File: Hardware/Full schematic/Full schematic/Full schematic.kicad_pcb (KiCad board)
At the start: 2 copper layers, 128 x 62.4 mm, 163 parts, among them J1 Conn_01x04_Male, J2 Conn_01x03_Male, J3 Conn_01x02_Male, J4 Conn_01x04_Male, J5 Conn_01x03_Male, J6 Conn_01x02_Male, J7 Conn_01x02_Male, J8 Conn_01x02_Male, J9 Conn_01x07_Male, K1 EDR101A0500, K2 EDR101A0500, K3 EDR101A0500, K4 EDR101A0500, K5 EDR101A0500, K6 EDR101A0500, Q1 BC847, Q10 IRLML2502, Q11 IRLML2502, Q12 IRLML2502, Q13 IRLML2502, Q2 BSS138, Q3 BC847, Q4 IRF610, Q5 BSS138, Q6 BFS17, Q7 AFT05MS003N, Q8 IRLML2502, Q9 IRLML2502, U1 74LVC2T45DC, U2 74LVC2T45DC, U3 AD9835, U4 ICS501, X1 50MHz

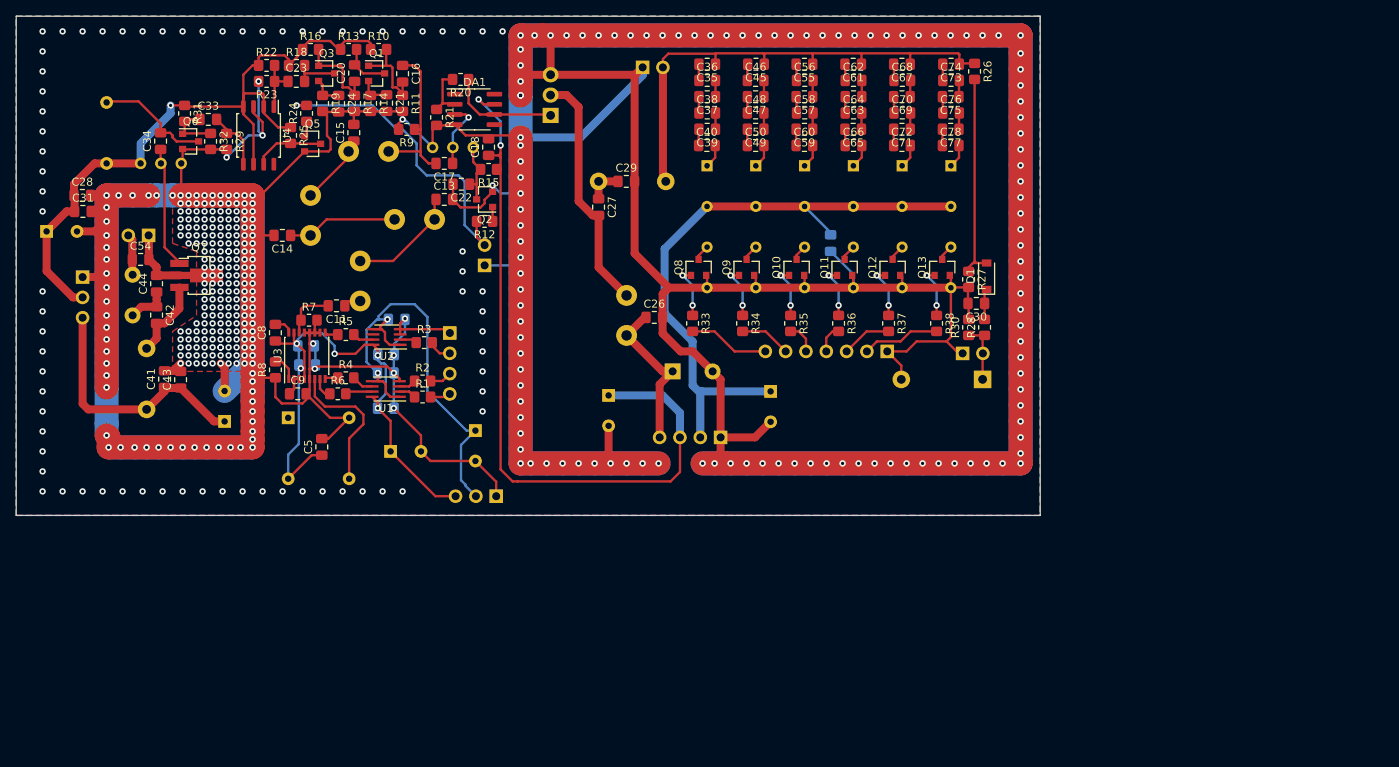
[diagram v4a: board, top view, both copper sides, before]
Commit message: Assigned cases to parts, ready to trace PCB
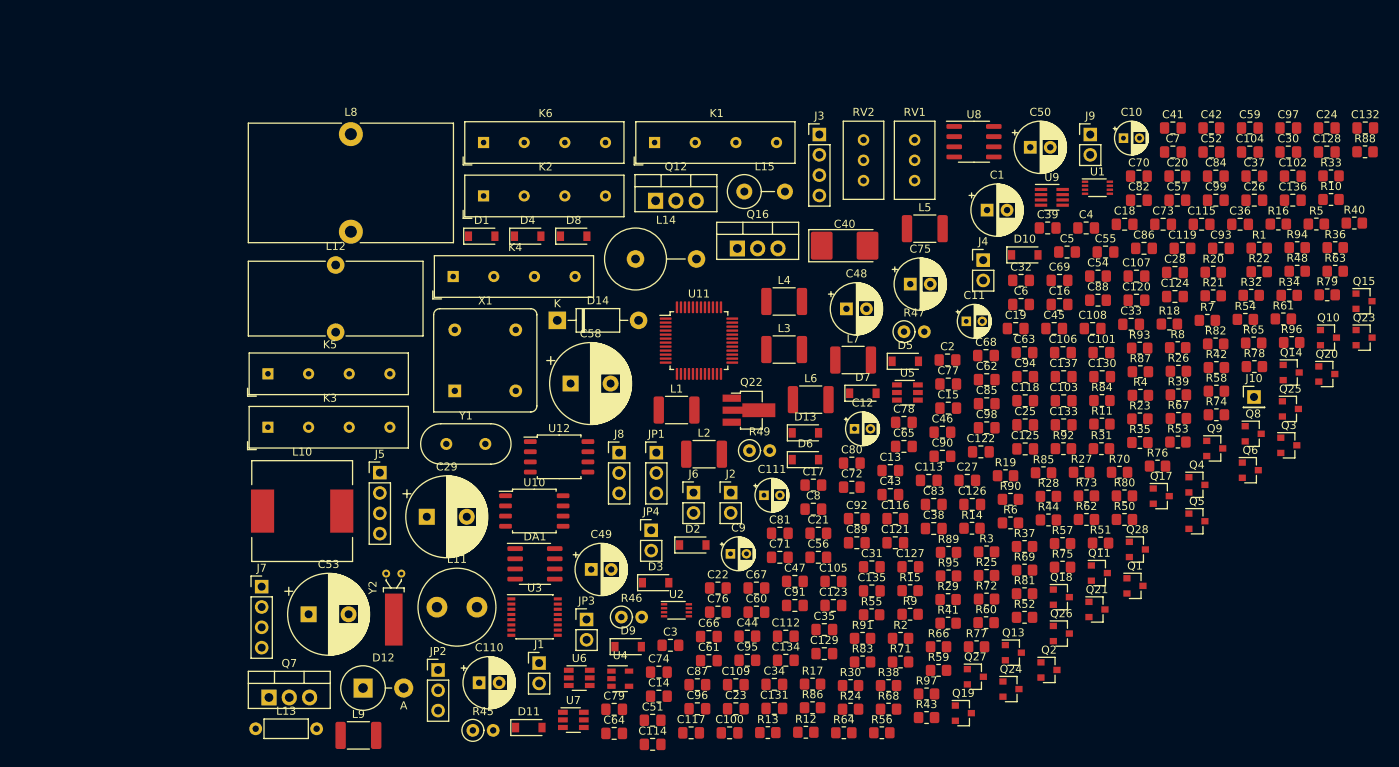
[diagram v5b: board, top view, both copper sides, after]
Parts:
- added C100: 0.1uF, Capacitor_SMD:C_0805_2012Metric_Pad1.18x1.45mm_HandSolder, F.Cu at (105.0, 106.0)
- added C101: 20pF, Capacitor_SMD:C_0805_2012Metric_Pad1.18x1.45mm_HandSolder, F.Cu at (151.5, 58.5)
- added C102: 200pF, Capacitor_SMD:C_0805_2012Metric_Pad1.18x1.45mm_HandSolder, F.Cu at (175.4, 36.4)
- added C103: 200pF, Capacitor_SMD:C_0805_2012Metric_Pad1.18x1.45mm_HandSolder, F.Cu at (146.7, 64.5)
- added C104: 200pF, Capacitor_SMD:C_0805_2012Metric_Pad1.18x1.45mm_HandSolder, F.Cu at (170.0, 33.4)
- added C105: 200pF, Capacitor_SMD:C_0805_2012Metric_Pad1.18x1.45mm_HandSolder, F.Cu at (117.9, 87.0)
- added C106: 200pF, Capacitor_SMD:C_0805_2012Metric_Pad1.18x1.45mm_HandSolder, F.Cu at (146.6, 58.5)
- added C107: 200pF, Capacitor_SMD:C_0805_2012Metric_Pad1.18x1.45mm_HandSolder, F.Cu at (155.8, 48.9)
- added C108: 0.1uF, Capacitor_SMD:C_0805_2012Metric_Pad1.18x1.45mm_HandSolder, F.Cu at (150.4, 55.4)
- added C109: 0.1uF, Capacitor_SMD:C_0805_2012Metric_Pad1.18x1.45mm_HandSolder, F.Cu at (105.8, 100.0)
- added C110: 100uF x 16V, Capacitor_THT:CP_Radial_D6.3mm_P2.50mm, F.Cu at (73.7, 99.7)
- added C111: 22uF x 10V, Capacitor_THT:CP_Radial_D4.0mm_P2.00mm, F.Cu at (109.3, 76.3)
- added C112: 0.1uF, Capacitor_SMD:C_0805_2012Metric_Pad1.18x1.45mm_HandSolder, F.Cu at (112.0, 93.9)
- added C113: 56pF, Capacitor_SMD:C_0805_2012Metric_Pad1.18x1.45mm_HandSolder, F.Cu at (129.9, 74.4)
- added C114: 100pF, Capacitor_SMD:C_0805_2012Metric_Pad1.18x1.45mm_HandSolder, F.Cu at (95.4, 107.4)
- added C115: 100pF, Capacitor_SMD:C_0805_2012Metric_Pad1.18x1.45mm_HandSolder, F.Cu at (164.0, 42.4)
- added C116: 100pF, Capacitor_SMD:C_0805_2012Metric_Pad1.18x1.45mm_HandSolder, F.Cu at (125.7, 79.2)
- added C117: 100pF, Capacitor_SMD:C_0805_2012Metric_Pad1.18x1.45mm_HandSolder, F.Cu at (100.2, 106.0)
- added C118: 100pF, Capacitor_SMD:C_0805_2012Metric_Pad1.18x1.45mm_HandSolder, F.Cu at (141.9, 64.5)
- added C119: 100pF, Capacitor_SMD:C_0805_2012Metric_Pad1.18x1.45mm_HandSolder, F.Cu at (161.6, 45.4)
- added C120: 47pF, Capacitor_SMD:C_0805_2012Metric_Pad1.18x1.45mm_HandSolder, F.Cu at (155.8, 51.9)
- added C121: 47pF, Capacitor_SMD:C_0805_2012Metric_Pad1.18x1.45mm_HandSolder, F.Cu at (125.7, 82.2)
- added C122: 47pF, Capacitor_SMD:C_0805_2012Metric_Pad1.18x1.45mm_HandSolder, F.Cu at (136.4, 70.9)
- added C123: 47pF, Capacitor_SMD:C_0805_2012Metric_Pad1.18x1.45mm_HandSolder, F.Cu at (117.9, 90.1)
- added C124: 47pF, Capacitor_SMD:C_0805_2012Metric_Pad1.18x1.45mm_HandSolder, F.Cu at (160.6, 51.4)
- added C125: 47pF, Capacitor_SMD:C_0805_2012Metric_Pad1.18x1.45mm_HandSolder, F.Cu at (141.9, 70.5)
- added C126: 24pF, Capacitor_SMD:C_0805_2012Metric_Pad1.18x1.45mm_HandSolder, F.Cu at (135.3, 77.4)
- added C127: 24pF, Capacitor_SMD:C_0805_2012Metric_Pad1.18x1.45mm_HandSolder, F.Cu at (127.6, 85.2)
- added C128: 24pF, Capacitor_SMD:C_0805_2012Metric_Pad1.18x1.45mm_HandSolder, F.Cu at (179.6, 33.4)
- added C129: 24pF, Capacitor_SMD:C_0805_2012Metric_Pad1.18x1.45mm_HandSolder, F.Cu at (116.8, 96.1)
- added C130: 24pF, Capacitor_SMD:C_0805_2012Metric_Pad1.18x1.45mm_HandSolder, F.Cu at (151.5, 61.5)
- added C131: 24pF, Capacitor_SMD:C_0805_2012Metric_Pad1.18x1.45mm_HandSolder, F.Cu at (110.6, 102.9)
- added C132: 12pF, Capacitor_SMD:C_0805_2012Metric_Pad1.18x1.45mm_HandSolder, F.Cu at (184.4, 30.4)
- added C133: 12pF, Capacitor_SMD:C_0805_2012Metric_Pad1.18x1.45mm_HandSolder, F.Cu at (146.7, 67.5)
- added C134: 12pF, Capacitor_SMD:C_0805_2012Metric_Pad1.18x1.45mm_HandSolder, F.Cu at (112.0, 96.9)
- added C135: 12pF, Capacitor_SMD:C_0805_2012Metric_Pad1.18x1.45mm_HandSolder, F.Cu at (122.8, 88.2)
- added C136: 12pF, Capacitor_SMD:C_0805_2012Metric_Pad1.18x1.45mm_HandSolder, F.Cu at (175.4, 39.4)
- added C137: 12pF, Capacitor_SMD:C_0805_2012Metric_Pad1.18x1.45mm_HandSolder, F.Cu at (146.7, 61.5)
- added C79: 22pF, Capacitor_SMD:C_0805_2012Metric_Pad1.18x1.45mm_HandSolder, F.Cu at (90.5, 103.0)
- added C80: 22pF, Capacitor_SMD:C_0805_2012Metric_Pad1.18x1.45mm_HandSolder, F.Cu at (120.3, 72.3)
- added C81: 10nF, Capacitor_SMD:C_0805_2012Metric_Pad1.18x1.45mm_HandSolder, F.Cu at (111.3, 81.0)
- added C82: 8pF, Capacitor_SMD:C_0805_2012Metric_Pad1.18x1.45mm_HandSolder, F.Cu at (156.1, 39.4)
- added C83: 8pF, Capacitor_SMD:C_0805_2012Metric_Pad1.18x1.45mm_HandSolder, F.Cu at (130.5, 77.4)
- added C84: 75pF, Capacitor_SMD:C_0805_2012Metric_Pad1.18x1.45mm_HandSolder, F.Cu at (165.8, 36.4)
- added C85: 4.7uF, Capacitor_SMD:C_0805_2012Metric_Pad1.18x1.45mm_HandSolder, F.Cu at (137.1, 64.8)
- added C86: 0.1uF, Capacitor_SMD:C_0805_2012Metric_Pad1.18x1.45mm_HandSolder, F.Cu at (156.8, 45.4)
- added C87: 390pF, Capacitor_SMD:C_0805_2012Metric_Pad1.18x1.45mm_HandSolder, F.Cu at (100.9, 100.0)
- added C88: 390pF, Capacitor_SMD:C_0805_2012Metric_Pad1.18x1.45mm_HandSolder, F.Cu at (151.0, 51.9)
- added C89: 390pF, Capacitor_SMD:C_0805_2012Metric_Pad1.18x1.45mm_HandSolder, F.Cu at (120.9, 82.2)
- added C90: 390pF, Capacitor_SMD:C_0805_2012Metric_Pad1.18x1.45mm_HandSolder, F.Cu at (131.6, 71.4)
- added C91: 390pF, Capacitor_SMD:C_0805_2012Metric_Pad1.18x1.45mm_HandSolder, F.Cu at (113.1, 90.1)
- added C92: 390pF, Capacitor_SMD:C_0805_2012Metric_Pad1.18x1.45mm_HandSolder, F.Cu at (120.9, 79.2)
- added C93: 10nF, Capacitor_SMD:C_0805_2012Metric_Pad1.18x1.45mm_HandSolder, F.Cu at (166.4, 45.4)
- added C94: 0.1uF, Capacitor_SMD:C_0805_2012Metric_Pad1.18x1.45mm_HandSolder, F.Cu at (141.9, 61.5)
- added C95: 10nF, Capacitor_SMD:C_0805_2012Metric_Pad1.18x1.45mm_HandSolder, F.Cu at (107.2, 96.9)
- added C96: 1nF, Capacitor_SMD:C_0805_2012Metric_Pad1.18x1.45mm_HandSolder, F.Cu at (100.9, 103.0)
- added C97: 1nF, Capacitor_SMD:C_0805_2012Metric_Pad1.18x1.45mm_HandSolder, F.Cu at (174.8, 30.4)
- added C98: 0.1uF, Capacitor_SMD:C_0805_2012Metric_Pad1.18x1.45mm_HandSolder, F.Cu at (137.1, 67.8)
- added C99: 0.1uF, Capacitor_SMD:C_0805_2012Metric_Pad1.18x1.45mm_HandSolder, F.Cu at (165.8, 39.4)
- added D10: 1N4148W, Diode_SMD:D_SOD-123, F.Cu at (141.9, 46.2)
- added D11: 1N4148W, Diode_SMD:D_SOD-123, F.Cu at (79.9, 105.3)
- added D12: 1N5819, Diode_THT:D_DO-27_P5.08mm_Vertical_AnodeUp, F.Cu at (59.2, 100.4)
- added D13: 1N4148W, Diode_SMD:D_SOD-123, F.Cu at (114.4, 68.5)
- added D14: 1N4728A, Diode_THT:D_DO-41_SOD81_P10.16mm_Horizontal, F.Cu at (83.4, 54.4)
- added D3: 1N4148W, Diode_SMD:D_SOD-123, F.Cu at (95.7, 87.2)
- added D4: MBR0520, Diode_SMD:D_SOD-123, F.Cu at (79.7, 43.9)
- added D5: MBR0520, Diode_SMD:D_SOD-123, F.Cu at (126.9, 59.5)
- added D6: MBR0520, Diode_SMD:D_SOD-123, F.Cu at (114.4, 71.8)
- added D7: MBR0520, Diode_SMD:D_SOD-123, F.Cu at (121.6, 63.5)
- added D8: 1N4148W, Diode_SMD:D_SOD-123, F.Cu at (85.5, 43.9)
- added D9: 1N4148W, Diode_SMD:D_SOD-123, F.Cu at (92.3, 95.2)
- added J10: Conn_01x01_Male, Connector_PinHeader_2.54mm:PinHeader_1x01_P2.54mm_Vertical, F.Cu at (170.5, 64.0)
- added JP1: BOOT0, Connector_PinHeader_2.54mm:PinHeader_1x03_P2.54mm_Vertical, F.Cu at (95.8, 71.0)
- added JP2: BOOT1, Connector_PinHeader_2.54mm:PinHeader_1x03_P2.54mm_Vertical, F.Cu at (68.5, 98.1)
- added JP3: SWDIO, Connector_PinHeader_2.54mm:PinHeader_1x02_P2.54mm_Vertical, F.Cu at (87.1, 91.8)
- added JP4: SWCLK, Connector_PinHeader_2.54mm:PinHeader_1x02_P2.54mm_Vertical, F.Cu at (95.2, 80.7)
- added L10: 150uH, Inductor_SMD:L_12x12mm_H8mm, F.Cu at (51.5, 78.3)
- added L11: 10uH, Inductor_THT:L_Radial_D9.5mm_P5.00mm_Fastron_07HVP, F.Cu at (68.4, 90.3)
- added L12: 21uH, Inductor_THT:L_Toroid_Vertical_L21.6mm_W9.1mm_P8.40mm_Bourns_5700, F.Cu at (55.7, 47.5)
- added L13: 200nH, Inductor_THT:L_Axial_L5.3mm_D2.2mm_P7.62mm_Horizontal_Vishay_IM-1, F.Cu at (45.7, 105.5)
- added L14: 300nH, Inductor_THT:L_Axial_L16.0mm_D7.5mm_P7.62mm_Vertical_Fastron_XHBCC, F.Cu at (93.2, 46.8)
- added L15: 23.5nH, Inductor_THT:L_Axial_L9.5mm_D4.0mm_P5.08mm_Vertical_Fastron_SMCC, F.Cu at (106.8, 38.3)
- added Q14: BSS138, Package_TO_SOT_SMD:SOT-23, F.Cu at (175.2, 60.9)
- added Q15: BC847, Package_TO_SOT_SMD:SOT-23, F.Cu at (184.3, 52.0)
- added Q16: IRF610, Package_TO_SOT_THT:TO-220-3_Vertical, F.Cu at (105.9, 45.4)
- added Q17: BC847, Package_TO_SOT_SMD:SOT-23, F.Cu at (158.9, 76.4)
- added Q18: IRLML6402, Package_TO_SOT_SMD:SOT-23, F.Cu at (146.4, 89.0)
- added Q19: BC847, Package_TO_SOT_SMD:SOT-23, F.Cu at (134.2, 103.5)
- added Q20: BFS17, Package_TO_SOT_SMD:SOT-23, F.Cu at (179.6, 61.1)
- added Q21: IRLML6402, Package_TO_SOT_SMD:SOT-23, F.Cu at (150.9, 90.6)
- added Q22: AFT05MS003N, Package_TO_SOT_SMD:SOT-89-3_Handsoldering, F.Cu at (107.4, 65.7)
- added Q23: IRLML2502, Package_TO_SOT_SMD:SOT-23, F.Cu at (184.3, 56.6)
- added Q24: IRLML2502, Package_TO_SOT_SMD:SOT-23, F.Cu at (140.1, 100.5)
- added Q25: IRLML2502, Package_TO_SOT_SMD:SOT-23, F.Cu at (175.1, 65.5)
- added Q26: IRLML2502, Package_TO_SOT_SMD:SOT-23, F.Cu at (146.4, 93.6)
- added Q27: IRLML2502, Package_TO_SOT_SMD:SOT-23, F.Cu at (135.7, 99.0)
- added Q28: IRLML2502, Package_TO_SOT_SMD:SOT-23, F.Cu at (155.9, 83.1)
- added R39: 10k, Resistor_SMD:R_0805_2012Metric_Pad1.20x1.40mm_HandSolder, F.Cu at (161.1, 63.7)
- added R40: 30k, Resistor_SMD:R_0805_2012Metric_Pad1.20x1.40mm_HandSolder, F.Cu at (183.1, 42.3)
- added R41: 10k, Resistor_SMD:R_0805_2012Metric_Pad1.20x1.40mm_HandSolder, F.Cu at (132.3, 92.3)
- added R42: 10, Resistor_SMD:R_0805_2012Metric_Pad1.20x1.40mm_HandSolder, F.Cu at (165.8, 60.3)
- added R43: 10k, Resistor_SMD:R_0805_2012Metric_Pad1.20x1.40mm_HandSolder, F.Cu at (129.6, 104.1)
- added R44: 1k, Resistor_SMD:R_0805_2012Metric_Pad1.20x1.40mm_HandSolder, F.Cu at (144.8, 79.4)
- added R45: 1, Resistor_THT:R_Axial_DIN0207_L6.3mm_D2.5mm_P2.54mm_Vertical, F.Cu at (72.9, 105.7)
- added R46: 1, Resistor_THT:R_Axial_DIN0207_L6.3mm_D2.5mm_P2.54mm_Vertical, F.Cu at (91.4, 91.5)
- added R47: 1, Resistor_THT:R_Axial_DIN0207_L6.3mm_D2.5mm_P2.54mm_Vertical, F.Cu at (126.8, 55.8)
- added R48: 4.7k, Resistor_SMD:R_0805_2012Metric_Pad1.20x1.40mm_HandSolder, F.Cu at (175.9, 48.3)
- added R49: 1, Resistor_THT:R_Axial_DIN0207_L6.3mm_D2.5mm_P2.54mm_Vertical, F.Cu at (107.5, 70.7)
- added R50: 30k, Resistor_SMD:R_0805_2012Metric_Pad1.20x1.40mm_HandSolder, F.Cu at (154.3, 79.3)
- added R51: 6.8k, Resistor_SMD:R_0805_2012Metric_Pad1.20x1.40mm_HandSolder, F.Cu at (151.3, 82.3)
- added R52: 100, Resistor_SMD:R_0805_2012Metric_Pad1.20x1.40mm_HandSolder, F.Cu at (141.8, 91.5)
- added R53: 1k, Resistor_SMD:R_0805_2012Metric_Pad1.20x1.40mm_HandSolder, F.Cu at (161.0, 69.6)
- added R54: 100, Resistor_SMD:R_0805_2012Metric_Pad1.20x1.40mm_HandSolder, F.Cu at (169.4, 54.3)
- added R55: 36k, Resistor_SMD:R_0805_2012Metric_Pad1.20x1.40mm_HandSolder, F.Cu at (122.7, 91.2)
- added R56: 4.3k, Resistor_SMD:R_0805_2012Metric_Pad1.20x1.40mm_HandSolder, F.Cu at (124.0, 106.0)
- added R57: 56k, Resistor_SMD:R_0805_2012Metric_Pad1.20x1.40mm_HandSolder, F.Cu at (146.6, 82.3)
- added R58: 30k, Resistor_SMD:R_0805_2012Metric_Pad1.20x1.40mm_HandSolder, F.Cu at (165.8, 63.3)
- added R59: 6.8k, Resistor_SMD:R_0805_2012Metric_Pad1.20x1.40mm_HandSolder, F.Cu at (131.1, 98.2)
- added R60: 1k, Resistor_SMD:R_0805_2012Metric_Pad1.20x1.40mm_HandSolder, F.Cu at (137.0, 92.2)
- added R61: 100, Resistor_SMD:R_0805_2012Metric_Pad1.20x1.40mm_HandSolder, F.Cu at (174.2, 54.2)
- added R62: 3.9k, Resistor_SMD:R_0805_2012Metric_Pad1.20x1.40mm_HandSolder, F.Cu at (149.6, 79.3)
- added R63: 2k, Resistor_SMD:R_0805_2012Metric_Pad1.20x1.40mm_HandSolder, F.Cu at (180.7, 48.3)
- added R64: 4.7k, Resistor_SMD:R_0805_2012Metric_Pad1.20x1.40mm_HandSolder, F.Cu at (119.3, 106.0)
- added R65: 4.7k, Resistor_SMD:R_0805_2012Metric_Pad1.20x1.40mm_HandSolder, F.Cu at (170.5, 57.2)
- added R66: 33k, Resistor_SMD:R_0805_2012Metric_Pad1.20x1.40mm_HandSolder, F.Cu at (131.1, 95.2)
- added R67: 4.7k, Resistor_SMD:R_0805_2012Metric_Pad1.20x1.40mm_HandSolder, F.Cu at (161.1, 66.7)
- added R68: 10k, Resistor_SMD:R_0805_2012Metric_Pad1.20x1.40mm_HandSolder, F.Cu at (124.8, 103.0)
- added R69: 10k, Resistor_SMD:R_0805_2012Metric_Pad1.20x1.40mm_HandSolder, F.Cu at (141.8, 85.6)
- added R70: 4.7k, Resistor_SMD:R_0805_2012Metric_Pad1.20x1.40mm_HandSolder, F.Cu at (153.7, 73.4)
- added R71: 220k, Resistor_SMD:R_0805_2012Metric_Pad1.20x1.40mm_HandSolder, F.Cu at (126.3, 97.1)
- added R72: 11k, Resistor_SMD:R_0805_2012Metric_Pad1.20x1.40mm_HandSolder, F.Cu at (137.1, 89.3)
- added R73: 4.7k, Resistor_SMD:R_0805_2012Metric_Pad1.20x1.40mm_HandSolder, F.Cu at (149.6, 76.4)
- added R74: 10, Resistor_SMD:R_0805_2012Metric_Pad1.20x1.40mm_HandSolder, F.Cu at (165.8, 66.2)
- added R75: 39k, Resistor_SMD:R_0805_2012Metric_Pad1.20x1.40mm_HandSolder, F.Cu at (146.6, 85.3)
- added R76: 33, Resistor_SMD:R_0805_2012Metric_Pad1.20x1.40mm_HandSolder, F.Cu at (158.5, 72.6)
- added R77: 10k, Resistor_SMD:R_0805_2012Metric_Pad1.20x1.40mm_HandSolder, F.Cu at (135.8, 95.2)
- added R78: 4.7k, Resistor_SMD:R_0805_2012Metric_Pad1.20x1.40mm_HandSolder, F.Cu at (170.6, 60.2)
- added R79: 10k, Resistor_SMD:R_0805_2012Metric_Pad1.20x1.40mm_HandSolder, F.Cu at (179.7, 51.2)
- added R80: 4.7k, Resistor_SMD:R_0805_2012Metric_Pad1.20x1.40mm_HandSolder, F.Cu at (154.3, 76.4)
- added R81: 10k, Resistor_SMD:R_0805_2012Metric_Pad1.20x1.40mm_HandSolder, F.Cu at (141.8, 88.6)
- added R82: 6.2k, Resistor_SMD:R_0805_2012Metric_Pad1.20x1.40mm_HandSolder, F.Cu at (165.7, 57.4)
- added R83: 1k, Resistor_SMD:R_0805_2012Metric_Pad1.20x1.40mm_HandSolder, F.Cu at (121.6, 97.1)
- added R84: 4.7k, Resistor_SMD:R_0805_2012Metric_Pad1.20x1.40mm_HandSolder, F.Cu at (151.5, 64.4)
- added R85: 10, Resistor_SMD:R_0805_2012Metric_Pad1.20x1.40mm_HandSolder, F.Cu at (144.2, 73.5)
- added R86: 4.7k, Resistor_SMD:R_0805_2012Metric_Pad1.20x1.40mm_HandSolder, F.Cu at (115.3, 102.8)
- added R87: 4.7k, Resistor_SMD:R_0805_2012Metric_Pad1.20x1.40mm_HandSolder, F.Cu at (156.3, 60.8)
- added R88: 4.7k, Resistor_SMD:R_0805_2012Metric_Pad1.20x1.40mm_HandSolder, F.Cu at (184.4, 33.4)
- added R89: 100, Resistor_SMD:R_0805_2012Metric_Pad1.20x1.40mm_HandSolder, F.Cu at (132.3, 83.4)
- added R90: 4.7k, Resistor_SMD:R_0805_2012Metric_Pad1.20x1.40mm_HandSolder, F.Cu at (140.1, 76.8)
- added R91: 4.7k, Resistor_SMD:R_0805_2012Metric_Pad1.20x1.40mm_HandSolder, F.Cu at (121.6, 94.2)
- added R92: 4.7k, Resistor_SMD:R_0805_2012Metric_Pad1.20x1.40mm_HandSolder, F.Cu at (146.7, 70.5)
- added R93: 100, Resistor_SMD:R_0805_2012Metric_Pad1.20x1.40mm_HandSolder, F.Cu at (156.2, 57.9)
- added R94: 100, Resistor_SMD:R_0805_2012Metric_Pad1.20x1.40mm_HandSolder, F.Cu at (175.9, 45.3)
- added R95: 100, Resistor_SMD:R_0805_2012Metric_Pad1.20x1.40mm_HandSolder, F.Cu at (132.3, 86.4)
- added R96: 100, Resistor_SMD:R_0805_2012Metric_Pad1.20x1.40mm_HandSolder, F.Cu at (175.2, 57.2)
- added R97: 100, Resistor_SMD:R_0805_2012Metric_Pad1.20x1.40mm_HandSolder, F.Cu at (129.6, 101.1)
- added U10: ICS501, Package_SO:SOIC-8_5.23x5.23mm_P1.27mm, F.Cu at (80.6, 78.2)
- added U11: STM32F103C8Tx, Package_QFP:LQFP-48_7x7mm_P0.5mm, F.Cu at (101.1, 57.0)
- added U12: CAT24C256, Package_SO:SOIC-8_5.23x5.23mm_P1.27mm, F.Cu at (83.7, 71.5)
- added U5: LM2734X, Package_TO_SOT_SMD:TSOT-23-6, F.Cu at (127.2, 63.4)
- added U6: LM2734X, Package_TO_SOT_SMD:TSOT-23-6, F.Cu at (86.2, 99.1)
- added U7: LM2734X, Package_TO_SOT_SMD:TSOT-23-6, F.Cu at (85.4, 104.4)
- added U8: UC3843_SOIC8, Package_SO:SOIC-8_3.9x4.9mm_P1.27mm, F.Cu at (135.5, 32.1)
- added U9: AD5245BRJZ10, Package_TO_SOT_SMD:SOT-23-8_Handsoldering, F.Cu at (145.3, 39.0)
- added Y1: 8MHz, Crystal:Crystal_HC49-U_Vertical, F.Cu at (69.6, 69.9)
- added Y2: 32768Hz, Crystal:Crystal_C26-LF_D2.1mm_L6.5mm_Horizontal_1EP_style1, F.Cu at (62.0, 86.1)
- C1: value 0.1uF -> 100uFx16V; footprint Capacitor_SMD:C_0805_2012Metric_Pad1.18x1.45mm_HandSolder -> Capacitor_THT:CP_Radial_D6.3mm_P2.50mm; moved to F.Cu
- C10: value 470uF x 6V -> 22uFx16V; footprint Capacitor_THT:CP_Radial_D8.0mm_P3.80mm -> Capacitor_THT:CP_Radial_D4.0mm_P2.00mm; moved to F.Cu
- C11: value 0.1uF -> 22uFx16V; footprint Capacitor_SMD:C_0805_2012Metric_Pad1.18x1.45mm_HandSolder -> Capacitor_THT:CP_Radial_D4.0mm_P2.00mm
- C12: value 470uF x 10V -> 22uFx16V; footprint Capacitor_THT:CP_Radial_D8.0mm_P3.80mm -> Capacitor_THT:CP_Radial_D4.0mm_P2.00mm; moved to F.Cu
- C13: value 47pF -> 1uF
- C14: value 56pF -> 4.7uF
- C15: value 47pF -> 4.7uF
- C16, C17, C23: value 0.1uF -> 4.7uF
- C19: value 470uFx16V -> 150pF; footprint Capacitor_THT:CP_Radial_D8.0mm_P3.80mm -> Capacitor_SMD:C_0805_2012Metric_Pad1.18x1.45mm_HandSolder; moved to F.Cu
- C2, C3, C4, C7, J6, K1, K2, K3, K4, K5, K6, RV1, RV2, X1: moved to F.Cu
- C20: value 0.1uF -> 220pF
- C21, C26, C27: value 0.1uF -> 10nF
- C25: value 1000uF x 25V -> 180pF; footprint Capacitor_THT:CP_Radial_D10.0mm_P5.00mm -> Capacitor_SMD:C_0805_2012Metric_Pad1.18x1.45mm_HandSolder; moved to F.Cu
- C28: value 1nF -> 10nF
- C29: value 75pF -> 1000uF x 10V; footprint Capacitor_SMD:C_0805_2012Metric_Pad1.18x1.45mm_HandSolder -> Capacitor_THT:CP_Radial_D10.0mm_P5.00mm
- C30: value 10nF -> 1nF
- C31: value 0.1uF -> 47pF
- C32: value 470uFx6.3V -> 10nF; footprint Capacitor_THT:CP_Radial_D8.0mm_P3.80mm -> Capacitor_SMD:C_0805_2012Metric_Pad1.18x1.45mm_HandSolder; moved to F.Cu
- C33: value 1nF -> 100pF
- C34: value 75pF -> 4.7uF
- C35: value 390pF -> 4.7uF
- C36: value 390pF -> 56pF
- C37, C38, C39: value 390pF -> 1nF
- C40: value 390pF -> 10uFx25V tantalum; footprint Capacitor_SMD:C_0805_2012Metric_Pad1.18x1.45mm_HandSolder -> Capacitor_Tantalum_SMD:CP_EIA-7132-28_AVX-C_Pad2.72x3.50mm_HandSolder
- C43: value 0.1uF -> 1nF
- C44: value 20pF -> 47pF
- C45, C46, C47: value 200pF -> 4.7uF
- C48, C49, C50: value 200pF -> 220uFx6.3V; footprint Capacitor_SMD:C_0805_2012Metric_Pad1.18x1.45mm_HandSolder -> Capacitor_THT:CP_Radial_D6.3mm_P2.50mm
- C51: value 470uF x 10V -> 1nF; footprint Capacitor_THT:CP_Radial_D8.0mm_P3.80mm -> Capacitor_SMD:C_0805_2012Metric_Pad1.18x1.45mm_HandSolder; moved to F.Cu
- C52: value 470uFx6.3V -> 4.7uF; footprint Capacitor_THT:CP_Radial_D8.0mm_P3.80mm -> Capacitor_SMD:C_0805_2012Metric_Pad1.18x1.45mm_HandSolder; moved to F.Cu
- C53: value 0.1uF -> 1000uF x 25V; footprint Capacitor_SMD:C_0805_2012Metric_Pad1.18x1.45mm_HandSolder -> Capacitor_THT:CP_Radial_D10.0mm_P5.00mm; moved to F.Cu
- C54: value 56pF -> 0.1uF
- C55: value 100pF -> 1nF
- C56, C59: value 100pF -> 0.1uF
- C57, C60: value 100pF -> 4.7uF
- C58: value 100pF -> 1000uF x 25V; footprint Capacitor_SMD:C_0805_2012Metric_Pad1.18x1.45mm_HandSolder -> Capacitor_THT:CP_Radial_D10.0mm_P5.00mm
- C6: value 0.1uF -> 1nF; moved to F.Cu
- C61, C62, C64, C65, C66: value 47pF -> 0.1uF
- C63: value 47pF -> 10nF
- C67: value 24pF -> 4.7uF
- C68, C69, C70: value 24pF -> 0.1uF
- C71: value 24pF -> 1nF
- C72: value 24pF -> 75pF
- C73, C76, C78: value 12pF -> 10nF
- C74: value 12pF -> 0.1uF
- C75: value 12pF -> 100uFx6.3V; footprint Capacitor_SMD:C_0805_2012Metric_Pad1.18x1.45mm_HandSolder -> Capacitor_THT:CP_Radial_D6.3mm_P2.50mm
- C77: value 12pF -> 1nF
- C8: value 10nF -> 0.1uF
- C9: value 10nF -> 22uFx16V; footprint Capacitor_SMD:C_0805_2012Metric_Pad1.18x1.45mm_HandSolder -> Capacitor_THT:CP_Radial_D4.0mm_P2.00mm
- D2: value 1N4728A -> 1N4148W; footprint Diode_THT:D_DO-41_SOD81_P10.16mm_Horizontal -> Diode_SMD:D_SOD-123; moved to F.Cu
- J1: value Conn_01x04_Male -> Conn_01x02_Male; footprint Connector_PinHeader_2.54mm:PinHeader_1x04_P2.54mm_Vertical -> Connector_PinHeader_2.54mm:PinHeader_1x02_P2.54mm_Vertical; moved to F.Cu
- J2: value Conn_01x03_Male -> Reset; footprint Connector_PinHeader_2.54mm:PinHeader_1x03_P2.54mm_Vertical -> Connector_PinHeader_2.54mm:PinHeader_1x02_P2.54mm_Vertical; moved to F.Cu
- J3: value Conn_01x02_Male -> Encoder; footprint Connector_PinHeader_2.54mm:PinHeader_1x02_P2.54mm_Vertical -> Connector_PinHeader_2.54mm:PinHeader_1x04_P2.54mm_Vertical; moved to F.Cu
- J4: value Conn_01x04_Male -> Failure LED; footprint Connector_PinHeader_2.54mm:PinHeader_1x04_P2.54mm_Vertical -> Connector_PinHeader_2.54mm:PinHeader_1x02_P2.54mm_Vertical; moved to F.Cu
- J5: value Conn_01x03_Male -> Bluetooth; footprint Connector_PinHeader_2.54mm:PinHeader_1x03_P2.54mm_Vertical -> Connector_PinHeader_2.54mm:PinHeader_1x04_P2.54mm_Vertical; moved to F.Cu
- J7: value Conn_01x02_Male -> Display; footprint Connector_PinHeader_2.54mm:PinHeader_1x02_P2.54mm_Vertical -> Connector_PinHeader_2.54mm:PinHeader_1x04_P2.54mm_Vertical; moved to F.Cu
- J8: value Conn_01x02_Male -> Buttons; footprint Connector_PinHeader_2.54mm:PinHeader_1x02_P2.54mm_Vertical -> Connector_PinHeader_2.54mm:PinHeader_1x03_P2.54mm_Vertical; moved to F.Cu
- J9: value Conn_01x07_Male -> Conn_01x02_Male; footprint Connector_PinHeader_2.54mm:PinHeader_1x07_P2.54mm_Vertical -> Connector_PinHeader_2.54mm:PinHeader_1x02_P2.54mm_Vertical; moved to F.Cu
- L1, L4: value 3.3uH -> 10uH; footprint Inductor_THT:L_Radial_D9.5mm_P5.00mm_Fastron_07HVP -> Inductor_SMD:L_1812_4532Metric_Pad1.30x3.40mm_HandSolder; moved to F.Cu
- L2: value 4.7uH -> 3.3uH; footprint Inductor_THT:L_Radial_D9.5mm_P5.00mm_Fastron_07HVP -> Inductor_SMD:L_1812_4532Metric_Pad1.30x3.40mm_HandSolder; moved to F.Cu
- L3: value 4.7uH -> 10uH; footprint Inductor_THT:L_Radial_D9.5mm_P5.00mm_Fastron_07HVP -> Inductor_SMD:L_1812_4532Metric_Pad1.30x3.40mm_HandSolder; moved to F.Cu
- L5: footprint Inductor_THT:L_Radial_D9.5mm_P5.00mm_Fastron_07HVP -> Inductor_SMD:L_1812_4532Metric_Pad1.30x3.40mm_HandSolder; moved to F.Cu
- L6: value 21uH -> 4.7uH; footprint Inductor_THT:L_Toroid_Vertical_L21.6mm_W9.1mm_P8.40mm_Bourns_5700 -> Inductor_SMD:L_1812_4532Metric_Pad1.30x3.40mm_HandSolder; moved to F.Cu
- L7: value 200nH -> 4.7uH; footprint Inductor_THT:L_Axial_L5.3mm_D2.2mm_P7.62mm_Horizontal_Vishay_IM-1 -> Inductor_SMD:L_1812_4532Metric_Pad1.30x3.40mm_HandSolder; moved to F.Cu
- L8: value 300nH -> 50uH; footprint Inductor_THT:L_Axial_L16.0mm_D7.5mm_P7.62mm_Vertical_Fastron_XHBCC -> Inductor_THT:L_Toroid_Vertical_L25.4mm_W14.7mm_P12.20mm_Vishay_TJ5_BigPads; moved to F.Cu
- L9: value 23.5nH -> 3.3uH; footprint Inductor_THT:L_Axial_L9.5mm_D4.0mm_P5.08mm_Vertical_Fastron_SMCC -> Inductor_SMD:L_1812_4532Metric_Pad1.30x3.40mm_HandSolder; moved to F.Cu
- Q10, Q8, Q9: value IRLML2502 -> IRLML6402
- Q11, Q13: value IRLML2502 -> BC847
- Q12: value IRLML2502 -> IRFZ44; footprint Package_TO_SOT_SMD:SOT-23 -> Package_TO_SOT_THT:TO-220-3_Vertical
- Q2, Q5: value BSS138 -> BC847
- Q4: value IRF610 -> BC847; footprint Package_TO_SOT_THT:TO-220-3_Vertical -> Package_TO_SOT_SMD:SOT-23; moved to F.Cu
- Q6: value BFS17 -> IRLML6402
- Q7: value AFT05MS003N -> IRF4905; footprint Package_TO_SOT_SMD:SOT-89-3_Handsoldering -> Package_TO_SOT_THT:TO-220-3_Vertical
- R10, R16: value 30k -> 10k
- R11, R17: value 6.8k -> 47k
- R12, R14, R37, R6: value 100 -> 10k
- R13: value 1k -> 10k
- R15: value 56k -> 10k
- R18: value 1k -> 10
- R19: value 100 -> 10
- R20: value 3.9k -> 10
- R21: value 2k -> 10
- R22: value 4.7k -> 10
- R23, R9: value 4.7k -> 10k
- R24: value 100 -> 4.7k
- R25: value 47k -> 100
- R26: value 220k -> 100
- R27: value 11k -> 100
- R28: value 39k -> 1.3k
- R29: value 33 -> 150k
- R30: value 10k -> 12k
- R31: value 6.2k -> 300
- R32: value 1k -> 13k
- R33: value 100 -> 3.9k
- R34: value 100 -> 120k
- R35: value 100 -> 13k
- R36: value 100 -> 51k
- R38: value 100 -> 39k
- R4, R5: value 100 -> 47k
- R7: value 300 -> 10k
- R8: value 3.9k -> 10k
- U1, U2: footprint Package_SO:SSOP-8_2.95x2.8mm_P0.65mm -> Package_SO:VSSOP-8_2.3x2mm_P0.5mm
- U4: value ICS501 -> LM27313XMF; footprint Package_SO:SOIC-8_5.23x5.23mm_P1.27mm -> Package_TO_SOT_SMD:SOT-23-5
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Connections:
- C1 pad 1: PWR_CMN_3.3 -> BATT_7.4V
- C10 pad 1: PWR_CMN_3.3 -> BATT_7.4V
- C11 pad 1: Net-(C11-Pad1) -> BATT_7.4V
- C11 pad 2: Net-(C11-Pad2) -> GND
- C12 pad 1: PWR_CMN_5 -> POWERS_3.5
- C14 pad 1: Net-(C14-Pad1) -> BATT_7.4V
- C15 pad 1: Net-(C15-Pad1) -> BATT_7.4V
- C16 pad 1: Net-(C16-Pad1) -> BATT_7.4V
- C16 pad 2: Net-(C16-Pad2) -> GND
- C17 pad 1: Net-(C17-Pad1) -> POWERS_3.5
- C17 pad 2: Net-(C16-Pad1) -> GND
- C18 pad 1: PWR_3.5_12 -> REG_5V
- C19 pad 1: PWR_3.5_12 -> Net-(C19-Pad1)
- C19 pad 2: GND -> Net-(C19-Pad2)
- C2 pad 1: PWR_CMN_3.3 -> REG_3.3V
- C20 pad 2: Net-(C20-Pad2) -> GND
- C21 pad 1: Net-(C21-Pad1) -> REG_5V
- C21 pad 2: GND -> Net-(C21-Pad2)
- C23 pad 1: Net-(C23-Pad1) -> PWR_3.5_12
- C23 pad 2: Net-(C23-Pad2) -> GND
- C24 pad 2: GND -> Net-(C24-Pad2)
- C25 pad 1: PWR_3.5_OUT -> PWR_3.5_12
- C25 pad 2: GND -> Net-(C25-Pad2)
- C26 pad 1: PWR_3.5_OUT -> Net-(C26-Pad1)
- C26 pad 2: GND -> Net-(C26-Pad2)
- C28 pad 1: PWR_144_5 -> Net-(C28-Pad1)
- C28 pad 2: GND -> Net-(C28-Pad2)
- C29 pad 1: Net-(C27-Pad1) -> POWERS_3.5
- C3 pad 1: PWR_CMN_5 -> REG_3.3V
- C30 pad 1: Net-(C30-Pad1) -> PWR_3.5_12
- C31 pad 1: PWR_144_5 -> Net-(C31-Pad1)
- C32 pad 1: PWR_144_5 -> Net-(C32-Pad1)
- C32 pad 2: GND -> Net-(C32-Pad2)
- C33 pad 1: Net-(C33-Pad1) -> Net-(C32-Pad1)
- C33 pad 2: Net-(C33-Pad2) -> GND
- C34 pad 1: Net-(C34-Pad1) -> POWERS_3.5
- C34 pad 2: Net-(C34-Pad2) -> GND
- C35 pad 1: ANT_3.5 -> PWR_3.5_12
- C35 pad 2: Net-(C35-Pad2) -> GND
- C36 pad 1: Net-(C35-Pad2) -> Net-(C36-Pad1)
- C36 pad 2: Net-(C36-Pad2) -> GND
- C37 pad 1: Net-(C36-Pad2) -> REG_5V
- C38 pad 1: Net-(C37-Pad2) -> DISPLAY_4V
- C39 pad 1: Net-(C38-Pad2) -> REG_3.3V
- C4 pad 1: PWR_CMN_5 -> REG_5V
- C40 pad 1: Net-(C39-Pad2) -> PWR_3.5_12
- C40 pad 2: Net-(C40-Pad2) -> GND
- C41 pad 1: PWR_144_OUT -> REG_5V
- C42 pad 1: Net-(C42-Pad1) -> DISPLAY_4V
- C42 pad 2: Net-(C42-Pad2) -> GND
- C43 pad 1: PWR_144_OUT -> REG_3.3V
- C44 pad 1: Net-(C42-Pad1) -> Net-(C44-Pad1)
- C45 pad 1: ANT_3.5 -> REG_5V
- C45 pad 2: Net-(C45-Pad2) -> GND
- C46 pad 1: Net-(C45-Pad2) -> DISPLAY_4V
- C46 pad 2: Net-(C46-Pad2) -> GND
- C47 pad 1: Net-(C46-Pad2) -> REG_3.3V
- C47 pad 2: Net-(C47-Pad2) -> GND
- C48 pad 1: Net-(C47-Pad2) -> REG_5V
- C48 pad 2: Net-(C48-Pad2) -> GND
- C49 pad 1: Net-(C48-Pad2) -> DISPLAY_4V
- C49 pad 2: Net-(C49-Pad2) -> GND
- C5 pad 1: PWR_CMN_5 -> REG_5V
- C50 pad 1: Net-(C49-Pad2) -> REG_3.3V
- C50 pad 2: Net-(C50-Pad2) -> GND
- C51 pad 1: PWR_144_OUT -> Net-(C51-Pad1)
- C52 pad 1: PWR_3.5_5 -> Net-(C51-Pad1)
- C53 pad 1: PWR_3.5_5 -> Net-(C51-Pad1)
- C54 pad 2: GND -> Net-(C54-Pad2)
- C55 pad 1: ANT_3.5 -> PWR_3.5_OUT
- C55 pad 2: Net-(C55-Pad2) -> GND
- C56 pad 1: Net-(C55-Pad2) -> Net-(C56-Pad1)
- C56 pad 2: Net-(C56-Pad2) -> Net-(C54-Pad1)
- C57 pad 1: Net-(C56-Pad2) -> PWR_3.5_OUT
- C57 pad 2: Net-(C57-Pad2) -> GND
- C58 pad 1: Net-(C57-Pad2) -> PWR_3.5_OUT
- C58 pad 2: Net-(C58-Pad2) -> GND
- C59 pad 1: Net-(C58-Pad2) -> PWR_3.5_12
- C59 pad 2: Net-(C59-Pad2) -> GND
- C6 pad 1: PWR_CMN_5 -> ADC_UBATT
- C60 pad 1: Net-(C59-Pad2) -> PWR_3.5_12
- C60 pad 2: Net-(C60-Pad2) -> GND
- C61 pad 1: ANT_3.5 -> Net-(C61-Pad1)
- C62 pad 1: Net-(C61-Pad2) -> Net-(C62-Pad1)
- C62 pad 2: Net-(C62-Pad2) -> GND
- C63 pad 1: Net-(C62-Pad2) -> Net-(C63-Pad1)
- C63 pad 2: Net-(C63-Pad2) -> GND
- C64 pad 1: Net-(C63-Pad2) -> REG_3.3V
- C64 pad 2: Net-(C64-Pad2) -> GND
- C65 pad 1: Net-(C64-Pad2) -> Net-(C65-Pad1)
- C66 pad 1: Net-(C65-Pad2) -> Net-(C66-Pad1)
- C66 pad 2: Net-(C66-Pad2) -> GND
- C67 pad 1: ANT_3.5 -> PWR_3.5_OUT
- C67 pad 2: Net-(C67-Pad2) -> GND
- C68 pad 1: Net-(C67-Pad2) -> PWR_3.5_OUT
- C68 pad 2: Net-(C68-Pad2) -> GND
- C69 pad 1: Net-(C68-Pad2) -> Net-(C69-Pad1)
- C7 pad 1: PWR_CMN_5 -> REG_5V
- C70 pad 1: Net-(C69-Pad2) -> RESET
- C70 pad 2: Net-(C70-Pad2) -> GND
- C71 pad 1: Net-(C70-Pad2) -> PWR_144_5
- C71 pad 2: Net-(C71-Pad2) -> GND
- C72 pad 1: Net-(C71-Pad2) -> Net-(C69-Pad1)
- C72 pad 2: Net-(C72-Pad2) -> GND
- C73 pad 1: ANT_3.5 -> Net-(C73-Pad1)
- C73 pad 2: Net-(C73-Pad2) -> GND
- C74 pad 1: Net-(C73-Pad2) -> PWR_144_5
- C74 pad 2: Net-(C74-Pad2) -> GND
- C75 pad 1: Net-(C74-Pad2) -> PWR_144_5
- C75 pad 2: Net-(C75-Pad2) -> GND
- C76 pad 1: Net-(C75-Pad2) -> ENCODER_BTN
- C76 pad 2: Net-(C76-Pad2) -> GND
- C77 pad 1: Net-(C76-Pad2) -> Net-(C77-Pad1)
- C78 pad 1: Net-(C77-Pad2) -> ENCODER_R
- C78 pad 2: Net-(C78-Pad2) -> GND
- C8 pad 1: PWR_CMN_5 -> REG_5V
- C8 pad 2: Net-(C8-Pad2) -> GND
- C9 pad 1: Net-(C9-Pad1) -> BATT_7.4V
- D1 pad 1: Net-(C30-Pad1) -> COMM_5V_ENABLE
- D1 pad 2: Net-(D1-Pad2) -> ACTIVATE_FOX
- D2 pad 1: Net-(D2-Pad1) -> COMM_5V_ENABLE
- D2 pad 2: GND -> ACTIVATE_3.5
- DA1 pad 3: Net-(C17-Pad1) -> Net-(C56-Pad1)
- J1 pad 1: GND -> BATT_7.4V
- J1 pad 2: Net-(J1-Pad2) -> GND
- J2 pad 1: GND -> RESET
- J2 pad 2: PWR_CMN_3.3 -> GND
- J3 pad 1: GND -> ENCODER_L
- J3 pad 2: Manipulation -> ENCODER_R
- J4 pad 1: GND -> FAIL_LED
- J4 pad 2: PWR_3.5_5 -> GND
- J5 pad 1: GND -> BT_5V
- J5 pad 2: PWR_144_5 -> GND
- J5 pad 3: PWR_144_OUT -> BT_RX
- J6 pad 2: Net-(D2-Pad1) -> ANT_3.5
- J7 pad 2: ANT_3.5 -> DISPLAY_4V
- J8 pad 1: GND -> BTN_LEFT
- J8 pad 2: Net-(C54-Pad1) -> BTN_RIGHT
- J9 pad 2: Net-(J9-Pad2) -> Net-(C113-Pad1)
- K1 pad 1: Net-(C40-Pad2) -> Net-(C92-Pad2)
- K2 pad 1: Net-(C50-Pad2) -> Net-(C107-Pad2)
- K3 pad 1: Net-(C60-Pad2) -> Net-(C119-Pad2)
- K4 pad 1: Net-(C66-Pad2) -> Net-(C125-Pad2)
- K5 pad 1: Net-(C72-Pad2) -> Net-(C131-Pad2)
- K6 pad 1: Net-(C78-Pad2) -> Net-(C137-Pad2)
- L1 pad 1: Net-(C11-Pad1) -> POWERS_3.5
- L1 pad 2: Net-(C13-Pad1) -> Net-(D4-Pad2)
- L2 pad 1: Net-(C13-Pad1) -> Net-(C24-Pad1)
- L2 pad 2: Net-(C14-Pad1) -> Net-(C31-Pad1)
- L3 pad 1: Net-(C14-Pad1) -> Net-(C26-Pad1)
- L3 pad 2: Net-(C15-Pad1) -> REG_5V
- L4 pad 1: Net-(C15-Pad1) -> Net-(C27-Pad1)
- L4 pad 2: Net-(C16-Pad1) -> DISPLAY_4V
- L5 pad 1: PWR_3.5_OUT -> Net-(C28-Pad1)
- L5 pad 2: Net-(C27-Pad2) -> REG_3.3V
- L6 pad 1: Net-(C27-Pad1) -> Net-(C31-Pad1)
- L6 pad 2: ANT_3.5 -> Net-(C36-Pad1)
- L7 pad 1: PWR_144_5 -> Net-(C36-Pad1)
- L7 pad 2: Net-(C34-Pad2) -> Net-(C44-Pad1)
- L8 pad 1: PWR_144_OUT -> POWERS_3.5
- L8 pad 2: Net-(C42-Pad2) -> Net-(D12-Pad2)
- L9 pad 1: Net-(C42-Pad1) -> Net-(C44-Pad1)
- Q1 pad 1: Net-(C16-Pad2) -> Net-(Q1-Pad1)
- Q1 pad 2: Net-(C21-Pad1) -> GND
- Q1 pad 3: Net-(C20-Pad2) -> Net-(Q1-Pad3)
- Q10 pad 2: GND -> REG_5V
- Q10 pad 3: Net-(K3-Pad5) -> PWR_144_5
- Q11 pad 1: Net-(Q11-Pad1) -> Net-(C20-Pad1)
- Q11 pad 2: GND -> Net-(Q11-Pad2)
- Q11 pad 3: Net-(K4-Pad5) -> Net-(C13-Pad1)
- Q12 pad 1: Net-(Q12-Pad1) -> Net-(D11-Pad2)
- Q12 pad 2: GND -> Net-(D12-Pad2)
- Q12 pad 3: Net-(K5-Pad5) -> Net-(Q12-Pad3)
- Q13 pad 1: Net-(Q13-Pad1) -> Net-(C54-Pad2)
- Q13 pad 2: GND -> Net-(C62-Pad1)
- Q13 pad 3: Net-(K6-Pad5) -> Net-(C61-Pad2)
- Q2 pad 3: Net-(C22-Pad1) -> Net-(Q2-Pad3)
- Q3 pad 1: Net-(C20-Pad1) -> Net-(Q3-Pad1)
- Q3 pad 2: Net-(C24-Pad1) -> GND
- Q3 pad 3: Net-(C23-Pad2) -> Net-(Q3-Pad3)
- Q4 pad 1: Net-(DA1-Pad6) -> Net-(Q4-Pad1)
- Q4 pad 2: Net-(C27-Pad2) -> GND
- Q4 pad 3: GND -> Net-(Q4-Pad3)
- Q6 pad 1: Net-(C33-Pad1) -> Net-(Q6-Pad1)
- Q6 pad 2: GND -> BATT_7.4V
- Q6 pad 3: Net-(C34-Pad2) -> Net-(Q6-Pad3)
- Q7 pad 1: Net-(C34-Pad1) -> Net-(Q7-Pad1)
- Q7 pad 2: GND -> POWERS_3.5
- Q7 pad 3: Net-(C42-Pad2) -> BATT_7.4V
- Q8 pad 2: GND -> REG_5V
- Q8 pad 3: Net-(K1-Pad5) -> PWR_3.5_5
- Q9 pad 2: GND -> BATT_7.4V
- Q9 pad 3: Net-(K2-Pad5) -> PWR_144_OUT
- R1 pad 2: Net-(J1-Pad4) -> DDS_SCLK
- R10 pad 1: PWR_144_5 -> Net-(Q5-Pad1)
- R10 pad 2: Net-(C16-Pad2) -> ACTIVATE_144
- R11 pad 1: Net-(C16-Pad2) -> ACTIVATE_144
- R12 pad 1: Net-(Q2-Pad1) -> BATT_7.4V
- R12 pad 2: Manipulation -> Net-(Q6-Pad1)
- R13 pad 1: PWR_144_5 -> BATT_7.4V
- R13 pad 2: Net-(C20-Pad2) -> Net-(Q7-Pad1)
- R14 pad 1: Net-(C21-Pad1) -> REG_5V
- R14 pad 2: GND -> Net-(Q8-Pad1)
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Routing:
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- removed copper zone on B.Cu, net GND
- removed copper zone on F.Cu, net GND
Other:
- board outline removed

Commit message: PCB tracing in progress
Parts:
- C23, C29, C53, C58, D12, L8, Q12, R45, R46, R47, R49: moved to B.Cu
- moved C52 156.6 mm to (59.1, 148.6), turned to 270 degrees
- moved C20 155.4 mm to (44.2, 138.9)
- moved C33 139.4 mm to (41.1, 135.1), turned to 270 degrees
- moved C57 135.5 mm to (80.6, 148.6), turned to 270 degrees
- moved U8 135.5 mm to (45.7, 133.6)
- moved C32 134.4 mm to (41.1, 138.9), turned to 270 degrees
- moved R42 132.6 mm to (53.0, 129.9), turned to 90 degrees
- moved R35 130.5 mm to (47.8, 142.2)
- moved C19 126.8 mm to (39.4, 131.6), turned to 270 degrees
- moved C55 126.5 mm to (78.1, 148.6), turned to 270 degrees
- moved U9 120.2 mm to (80.6, 140.3), turned to 90 degrees
- moved L8 119.4 mm to (40.0, 149.2), turned to 270 degrees
- moved Q11 116.5 mm to (47.8, 139.7), turned to 90 degrees
- moved R28 113.6 mm to (50.5, 139.7), turned to 90 degrees
- moved Q12 102.4 mm to (53.3, 132.7)
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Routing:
- net GND: track 0.00 -> 122.3 mm, vias 0 -> 2
- net Net-(C19-Pad2): track 0.00 -> 49.5 mm, vias 0 -> 2
- net POWERS_3.5: track 0.00 -> 36.3 mm
- net Net-(C32-Pad1): track 0.00 -> 23.4 mm, vias 0 -> 2
- net Net-(Q12-Pad3): track 0.00 -> 20.5 mm
- net Net-(C51-Pad1): track 0.00 -> 18.5 mm
- net Net-(D12-Pad2): track 0.00 -> 18.0 mm
- net Net-(C13-Pad1): track 0.00 -> 11.7 mm
- net PWR_3.5_OUT: track 0.00 -> 11.2 mm
- net Net-(D11-Pad1): track 0.00 -> 9.16 mm
- net Net-(C20-Pad1): track 0.00 -> 7.88 mm
- net Net-(C32-Pad2): track 0.00 -> 6.56 mm
- net Net-(D11-Pad2): track 0.00 -> 6.52 mm
- net Net-(R56-Pad2): track 0.00 -> 5.09 mm
- net Net-(C19-Pad1): track 0.00 -> 4.36 mm
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
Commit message: PCB tracing in progress
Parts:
- C1, C10, C11, C12, C48, C49, C50, C9, J1, Q7: moved to B.Cu
- moved C30 186.2 mm to (47.8, 169.4), turned to 270 degrees
- moved C26 174.0 mm to (61.5, 175.0), turned to 90 degrees
- moved R36 173.8 mm to (58.7, 169.2), turned to 180 degrees
- moved R34 173.1 mm to (45.0, 165.6), turned to 90 degrees
- moved C37 172.1 mm to (58.7, 167.1), turned to 180 degrees
- moved R32 170.4 mm to (42.9, 164.6), turned to 90 degrees
- moved C41 168.1 mm to (65.5, 169.2), turned to 90 degrees
- moved R20 165.0 mm to (68.3, 181.9)
- moved C10 163.0 mm to (69.6, 170.9), turned to 90 degrees
- moved C42 157.3 mm to (83.1, 164.6), turned to 90 degrees
- moved R40 155.3 mm to (88.4, 165.4), turned to 180 degrees
- moved Q8 155.2 mm to (63.2, 180.8), turned to 180 degrees
- moved Q3 152.3 mm to (68.6, 179.1), turned to 270 degrees
- moved R8 149.0 mm to (69.6, 175.5), turned to 90 degrees
- moved C50 140.4 mm to (94.2, 164.6), turned to 90 degrees
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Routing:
- net GND: track 122.3 -> 322.2 mm, vias 2 -> 4
- net BATT_7.4V: track 0.00 -> 86.2 mm
- net PWR_3.5_12: track 2.12 -> 65.8 mm, vias 1 -> 4
- net REG_3.3V: track 2.34 -> 63.7 mm, vias 0 -> 1
- net REG_5V: track 0.00 -> 44.0 mm, vias 0 -> 1
- net DISPLAY_4V: track 0.00 -> 24.2 mm
- net POWERS_3.5: track 36.3 -> 57.0 mm
- net Net-(Q2-Pad3): track 0.00 -> 12.1 mm
- net Net-(Q7-Pad1): track 0.00 -> 8.95 mm
- net Net-(C28-Pad1): track 0.00 -> 7.66 mm
- net Net-(C27-Pad1): track 0.00 -> 7.32 mm
- net Net-(C26-Pad1): track 0.00 -> 6.93 mm
- net Net-(C37-Pad2): track 0.00 -> 6.50 mm
- net Net-(C25-Pad2): track 0.00 -> 6.22 mm
- net Net-(D4-Pad2): track 0.00 -> 6.11 mm
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
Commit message: PCB tracing in progress
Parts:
- C111, C112, D14, K1, K2, K3, K4, K5, K6: moved to B.Cu
- moved K5 181.4 mm to (221.5, 111.5), turned to 270 degrees
- moved K6 172.4 mm to (227.3, 111.5), turned to 270 degrees
- moved K3 168.3 mm to (209.8, 111.5), turned to 270 degrees
- moved D14 159.4 mm to (231.6, 113.0), turned to 270 degrees
- moved K4 158.1 mm to (215.6, 111.5), turned to 270 degrees
- moved K2 148.7 mm to (204.0, 111.5), turned to 270 degrees
- moved K1 129.6 mm to (198.1, 111.5), turned to 270 degrees
- moved D13 122.5 mm to (231.9, 103.3), turned to 90 degrees
- moved C134 115.0 mm to (226.8, 103.6), turned to 180 degrees
- moved C114 114.2 mm to (209.3, 99.6), turned to 180 degrees
- moved C131 110.6 mm to (221.0, 109.7)
- moved C117 109.1 mm to (209.3, 105.7)
- moved C135 105.5 mm to (226.8, 105.7)
- moved C129 104.6 mm to (221.0, 105.7)
- moved C112 104.1 mm to (212.6, 120.7), turned to 270 degrees
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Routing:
- net GND: track 322.2 -> 404.5 mm
- net PWR_3.5_5: track 0.00 -> 40.2 mm
- net ANT_3.5: track 0.00 -> 31.2 mm, vias 0 -> 6
- net ADC_UANT: track 0.00 -> 4.27 mm
- net Net-(C73-Pad1): track 0.00 -> 3.95 mm
- net Net-(D13-Pad2): track 0.00 -> 3.86 mm
- net Net-(Q26-Pad1): track 0.00 -> 3.37 mm
- net Net-(Q25-Pad1): track 0.00 -> 3.37 mm
- net Net-(Q28-Pad1): track 0.00 -> 3.36 mm
- net Net-(Q27-Pad1): track 0.00 -> 3.31 mm
- net Net-(Q24-Pad1): track 0.00 -> 3.27 mm
- net Net-(Q23-Pad1): track 0.00 -> 3.23 mm
- net Net-(C103-Pad2): track 0.00 -> 2.05 mm
- net Net-(C104-Pad2): track 0.00 -> 2.05 mm
- net Net-(C88-Pad2): track 0.00 -> 2.04 mm
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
